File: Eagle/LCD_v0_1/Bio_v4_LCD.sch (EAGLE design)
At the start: 39 parts, among them X2 16MHz, X3 FH12-08S-1SH, X4 MINI-USB

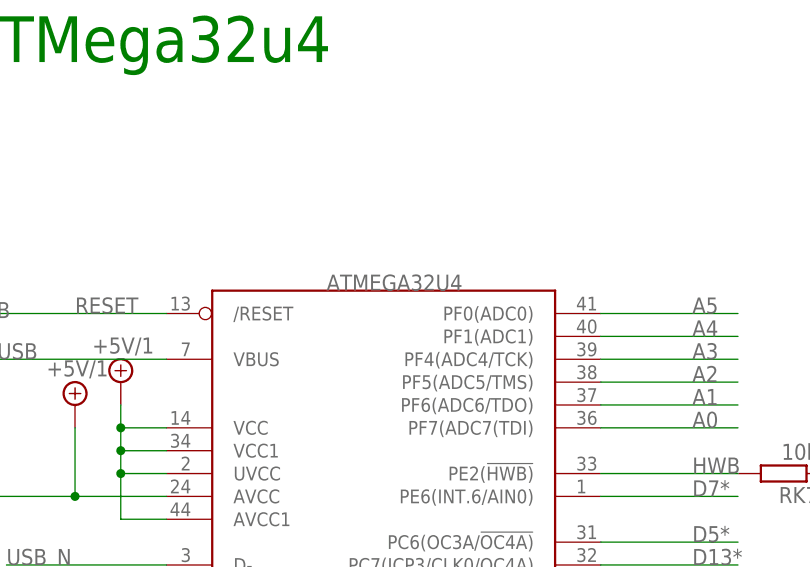
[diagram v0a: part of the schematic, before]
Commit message: Update value label position
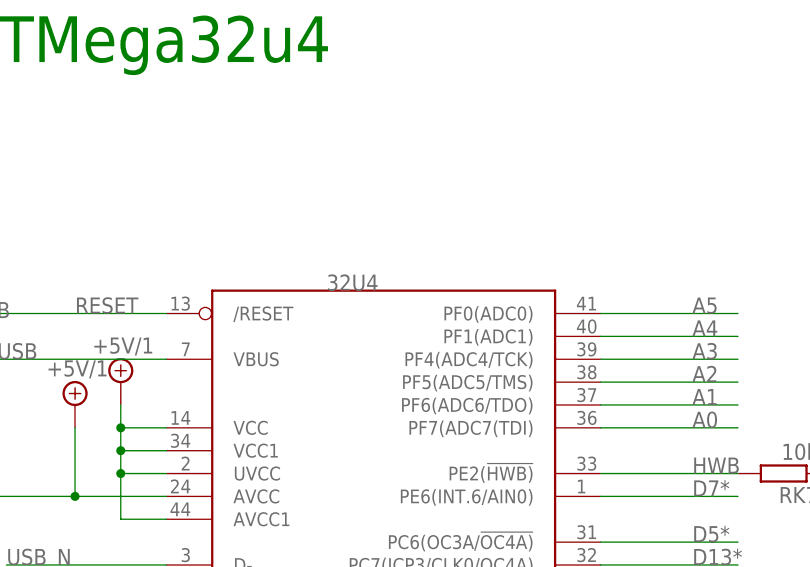
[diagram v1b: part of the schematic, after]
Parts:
- 32U4: value ATMEGA32U4 -> 32U4
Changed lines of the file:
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@@
 <?xml version="1.0" encoding="utf-8"?>
 <!DOCTYPE eagle SYSTEM "eagle.dtd">
-<eagle version="7.5.0">
+<eagle version="7.3.0">
 <drawing>
 <settings>
@@
 <part name="GND21" library="supply1" deviceset="GND" device=""/>
 <part name="C10" library="rcl" deviceset="C-EU" device="C1206" value="100nF"/>
-<part name="32U4" library="adafruit" deviceset="ATMEGA32U4" device="-AU" value="ATMEGA32U4"/>
+<part name="32U4" library="adafruit" deviceset="ATMEGA32U4" device="-AU" value="32U4"/>
 <part name="CX2" library="rcl" deviceset="C-EU" device="C1206" value="22pF"/>
 <part name="CX1" library="rcl" deviceset="C-EU" device="C1206" value="22pF"/>
